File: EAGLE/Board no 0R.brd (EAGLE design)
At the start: 100 x 70 mm, 166 parts, among them J1 JUMPER_SOLDER_1X2, J10 JUMPER_SOLDER_1X2, J11 JUMPER_SOLDER_1X2, J12 KF301-2P, J2 JUMPER_SOLDER_1X2, J3 JUMPER_SOLDER_1X2, J4 JUMPER_SOLDER_1X2, J5 JUMPER_SOLDER_1X2, J6 JUMPER_SOLDER_1X2, J8 KF301-2P, J9 JUMPER_SOLDER_1X2, Q1 500mA/300V, Q2 500mA/300V, Q3 FDN337N, Q4 FDN340P, U1 SN74HC04PW, U2 ESP32-WROOM-32, U3 CH340C, U4 AMS1117, U6 PCA9635PW, U7 SN74HC04PW, U8 SN74HC04PW, U9 LTC1694IS5#TRPBF, X1 JST-XH-04-PIN-LONG-PAD, X2 JST-XH-04-PIN-LONG-PAD

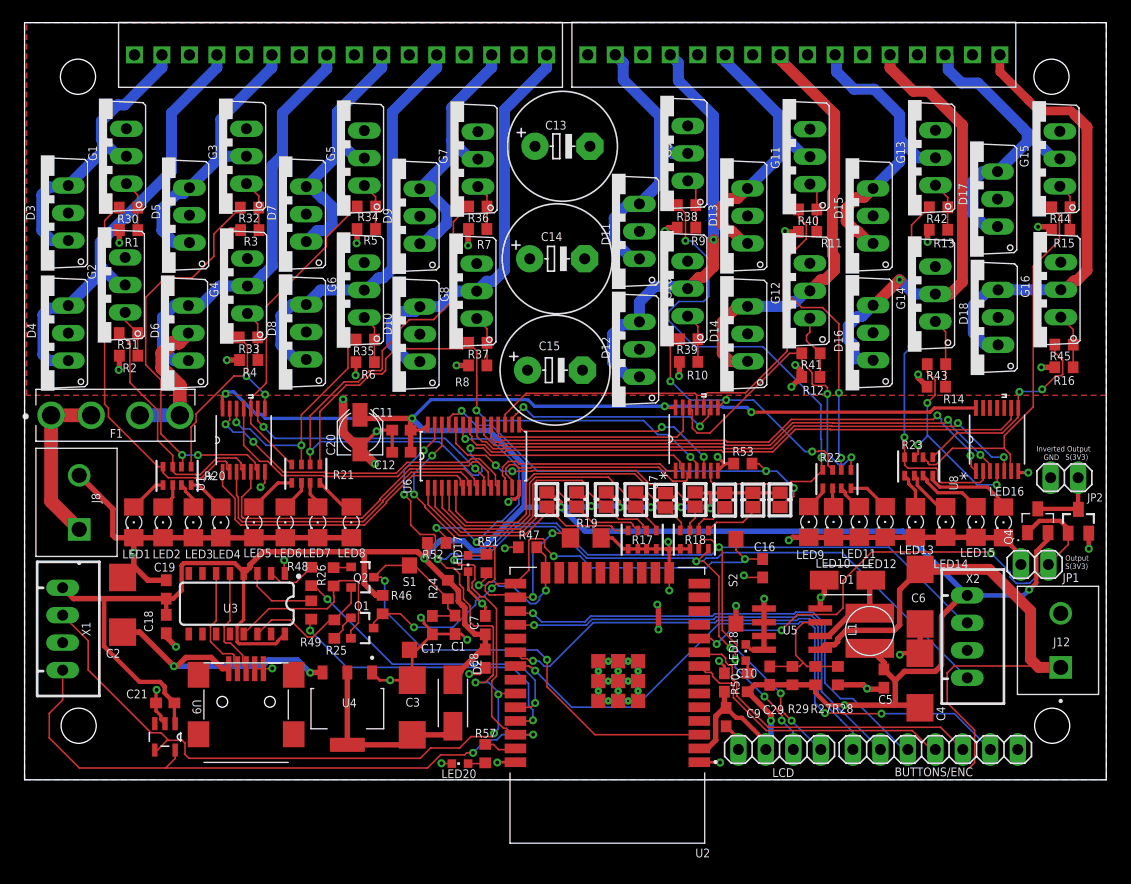
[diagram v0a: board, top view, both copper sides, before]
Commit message: Update EAGLE files to latest version
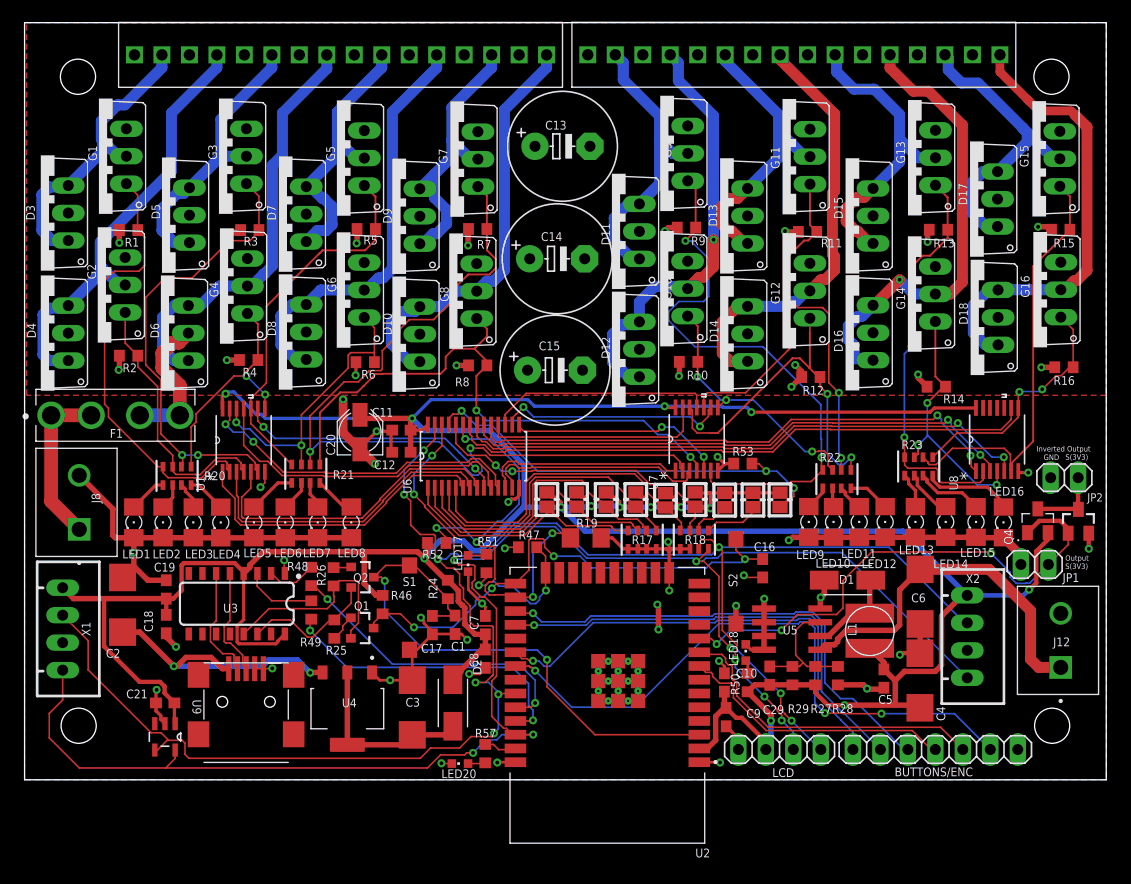
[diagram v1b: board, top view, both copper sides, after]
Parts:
- removed R30, R31, R32, R33, R34, R35, R36, R37, R38, R39, R40, R41, R42, R43, R44, R45: (no value), rcl:R0603
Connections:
- removed net N$26: G1.1, R1.2, R30.1
- removed net N$45: G2.1, R2.2, R31.1
- removed net N$47: G3.1, R3.2, R32.1
- removed net N$49: G4.1, R33.1, R4.2
- removed net N$51: G5.1, R34.1, R5.2
- removed net N$52: G6.1, R35.1, R6.2
- removed net N$53: G7.1, R36.1, R7.2
- removed net N$55: G8.1, R37.1, R8.2
- removed net N$56: G9.1, R38.1, R9.2
- removed net N$57: G10.1, R10.2, R39.1
- removed net N$58: G11.1, R11.2, R40.1
- removed net N$59: G12.1, R12.2, R41.1
- removed net N$60: G13.1, R13.2, R42.1
- removed net N$61: G14.1, R14.2, R43.1
- removed net N$62: G15.1, R15.2, R44.1
- removed net N$63: G16.1, R16.2, R45.1
- net SIG1: now also G1.1, R1.2; no longer R30.2
- net SIG10: now also G10.1, R10.2; no longer R39.2
- net SIG11: now also G11.1, R11.2; no longer R40.2
- net SIG12: now also G12.1, R12.2; no longer R41.2
- net SIG13: now also G13.1, R13.2; no longer R42.2
- net SIG14: now also G14.1, R14.2; no longer R43.2
- net SIG15: now also G15.1, R15.2; no longer R44.2
- net SIG16: now also G16.1, R16.2; no longer R45.2
- net SIG2: now also G2.1, R2.2; no longer R31.2
- net SIG3: now also G3.1, R3.2; no longer R32.2
- net SIG4: now also G4.1, R4.2; no longer R33.2
- net SIG5: now also G5.1, R5.2; no longer R34.2
- net SIG6: now also G6.1, R6.2; no longer R35.2
- net SIG7: now also G7.1, R7.2; no longer R36.2
- net SIG8: now also G8.1, R8.2; no longer R37.2
- net SIG9: now also G9.1, R9.2; no longer R38.2
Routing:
- net VDD: track 54.6 -> 33.7 mm
- net N$61: track 6.43 -> 0.00 mm
- net N$59: track 6.15 -> 0.00 mm
- net SIG5: track 29.5 -> 34.9 mm
- net SIG6: track 21.8 -> 27.2 mm
- net SIG1: track 35.4 -> 40.6 mm
- net N$63: track 5.11 -> 0.00 mm
- net N$47: track 4.77 -> 0.00 mm
- net SIG7: track 73.7 -> 78.4 mm
- net N$26: track 4.73 -> 0.00 mm
- net N$55: track 4.73 -> 0.00 mm
- net N$49: track 4.70 -> 0.00 mm
- net N$58: track 4.69 -> 0.00 mm
- net N$56: track 4.63 -> 0.00 mm
- net N$57: track 4.63 -> 0.00 mm
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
